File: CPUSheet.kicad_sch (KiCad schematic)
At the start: 13 parts, among them U1 80486DX, U2 7400, U3 7400

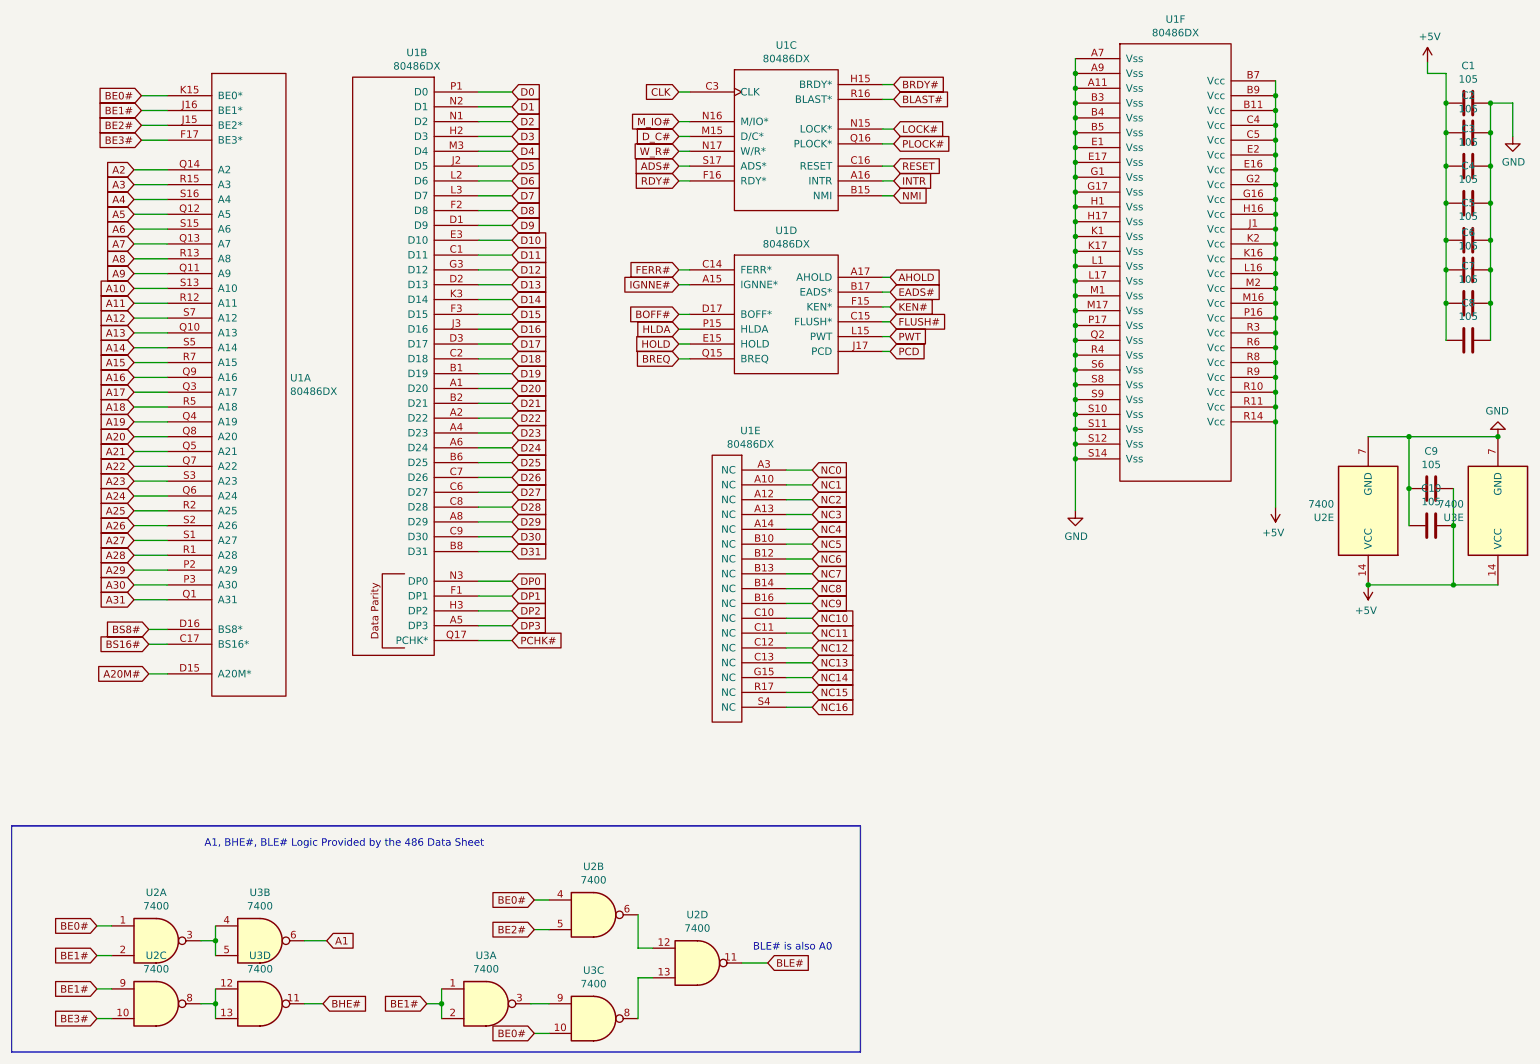
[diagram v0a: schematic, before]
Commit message: Updating the 486 Breakout Board
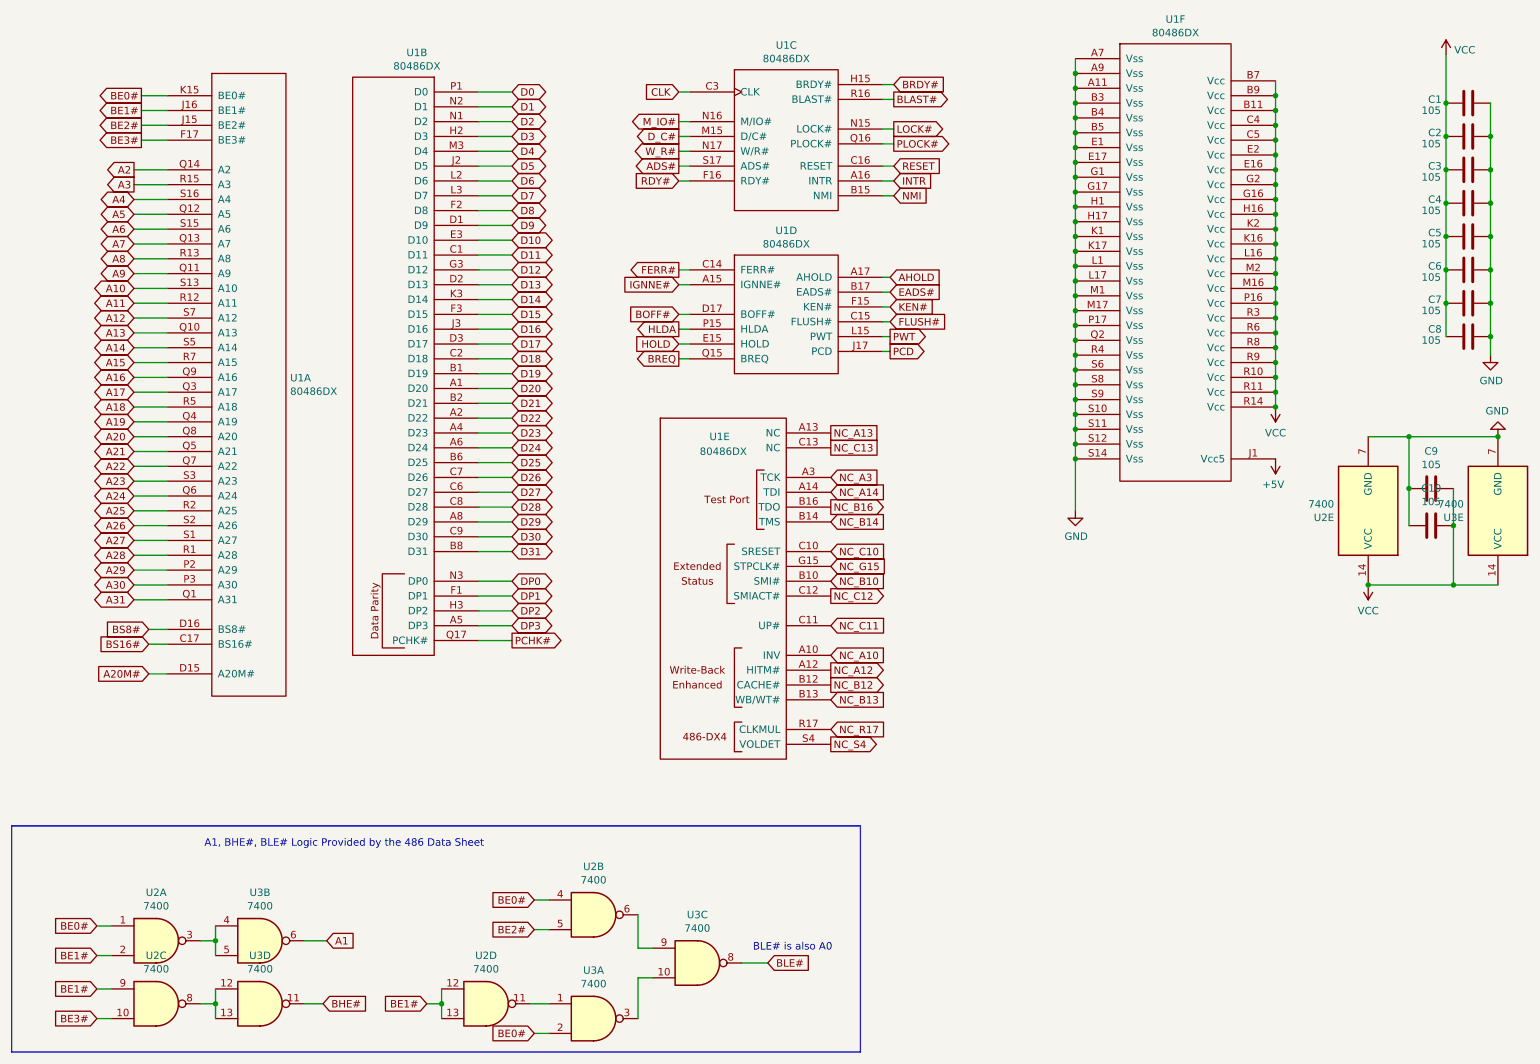
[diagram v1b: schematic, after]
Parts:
- C1, C2, C3, C4, C5, C6, C7, C8: footprint Capacitor_THT:C_Disc_D3.0mm_W1.6mm_P2.50mm -> Capacitor_SMD:C_0805_2012Metric_Pad1.18x1.45mm_HandSolder
- C10, C9: footprint Capacitor_THT:C_Disc_D3.0mm_W1.6mm_P2.50mm -> Capacitor_THT:C_Disc_D3.4mm_W2.1mm_P2.50mm
- U1: symbol 486:80486 -> 80486:80486
- U2, U3: footprint Package_DIP:DIP-14_W7.62mm_Socket -> Package_DIP:DIP-14_W7.62mm
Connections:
- net +5V: no longer C1.2, C10.1, C2.2, C3.2, C4.2, C5.2, C6.2, C7.2, C8.2, C9.1, U1.B11 (Vcc), U1.B7 (Vcc), U1.B9 (Vcc), U1.C4 (Vcc), U1.C5 (Vcc), U1.E16 (Vcc), U1.E2 (Vcc), U1.G16 (Vcc), U1.G2 (Vcc), U1.H16 (Vcc), U1.K16 (Vcc), U1.K2 (Vcc), U1.L16 (Vcc), U1.M16 (Vcc), U1.M2 (Vcc), U1.P16 (Vcc), U1.R10 (Vcc), U1.R11 (Vcc), U1.R14 (Vcc), U1.R3 (Vcc), U1.R6 (Vcc), U1.R8 (Vcc), U1.R9 (Vcc), U2.14 (VCC), U3.14 (VCC)
- net BE0#: now also U3.2; no longer U3.10
- net BE1#: now also U2.12, U2.13; no longer U3.1, U3.2
- net BLE#: now also U3.8; no longer U2.11
- net at U3.3: now also U3.10; no longer U3.9
- net at U2.6: now also U3.9; no longer U2.12
- net NC0 renamed NC_A3
- net NC1 renamed NC_A10
- net NC10 renamed NC_C10
- net NC11 renamed NC_C11
- net NC12 renamed NC_C12
- net NC13 renamed NC_C13
- net NC14 renamed NC_G15
- net NC15 renamed NC_R17
- net NC16 renamed NC_S4
- net NC2 renamed NC_A12
- net NC3 renamed NC_A13
- net NC4 renamed NC_A14
- net NC5 renamed NC_B10
- net NC6 renamed NC_B12
- net NC7 renamed NC_B13
- net NC8 renamed NC_B14
- net NC9 renamed NC_B16
- new net: U2.11, U3.1
- new net VCC: C1.2, C10.1, C2.2, C3.2, C4.2, C5.2, C6.2, C7.2, C8.2, C9.1, U1.B11 (Vcc), U1.B7 (Vcc), U1.B9 (Vcc), U1.C4 (Vcc), U1.C5 (Vcc), U1.E16 (Vcc), U1.E2 (Vcc), U1.G16 (Vcc), U1.G2 (Vcc), U1.H16 (Vcc), U1.K16 (Vcc), U1.K2 (Vcc), U1.L16 (Vcc), U1.M16 (Vcc), U1.M2 (Vcc), U1.P16 (Vcc), U1.R10 (Vcc), U1.R11 (Vcc), U1.R14 (Vcc), U1.R3 (Vcc), U1.R6 (Vcc), U1.R8 (Vcc), U1.R9 (Vcc), U2.14 (VCC), U3.14 (VCC)
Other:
- moved on the sheet: C2, C3, C5, C8, U2D, U3A, U3C
